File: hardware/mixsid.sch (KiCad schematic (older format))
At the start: 71 parts, among them P1 INPUT, P2 CONTROL, P3 RAW, P4 SOCKET LEFT, P5 OUTPUT, P6 SOCKET RIGHT, P7 -5V, Q1 BC547, Q2 BC547, U1 GAL16V8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

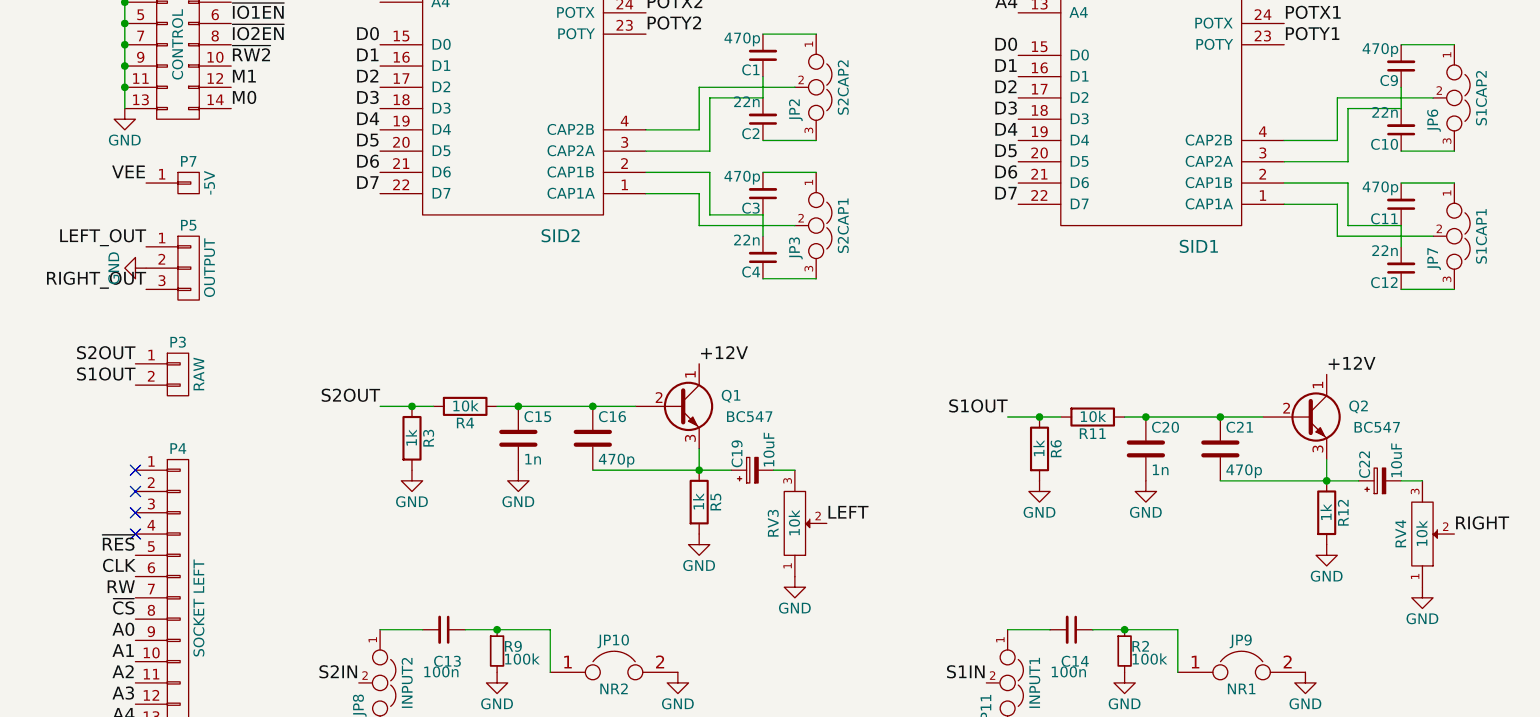
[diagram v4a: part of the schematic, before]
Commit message: Hardware: Added R8 Jumpers, Feed SID specific VDD into output stages
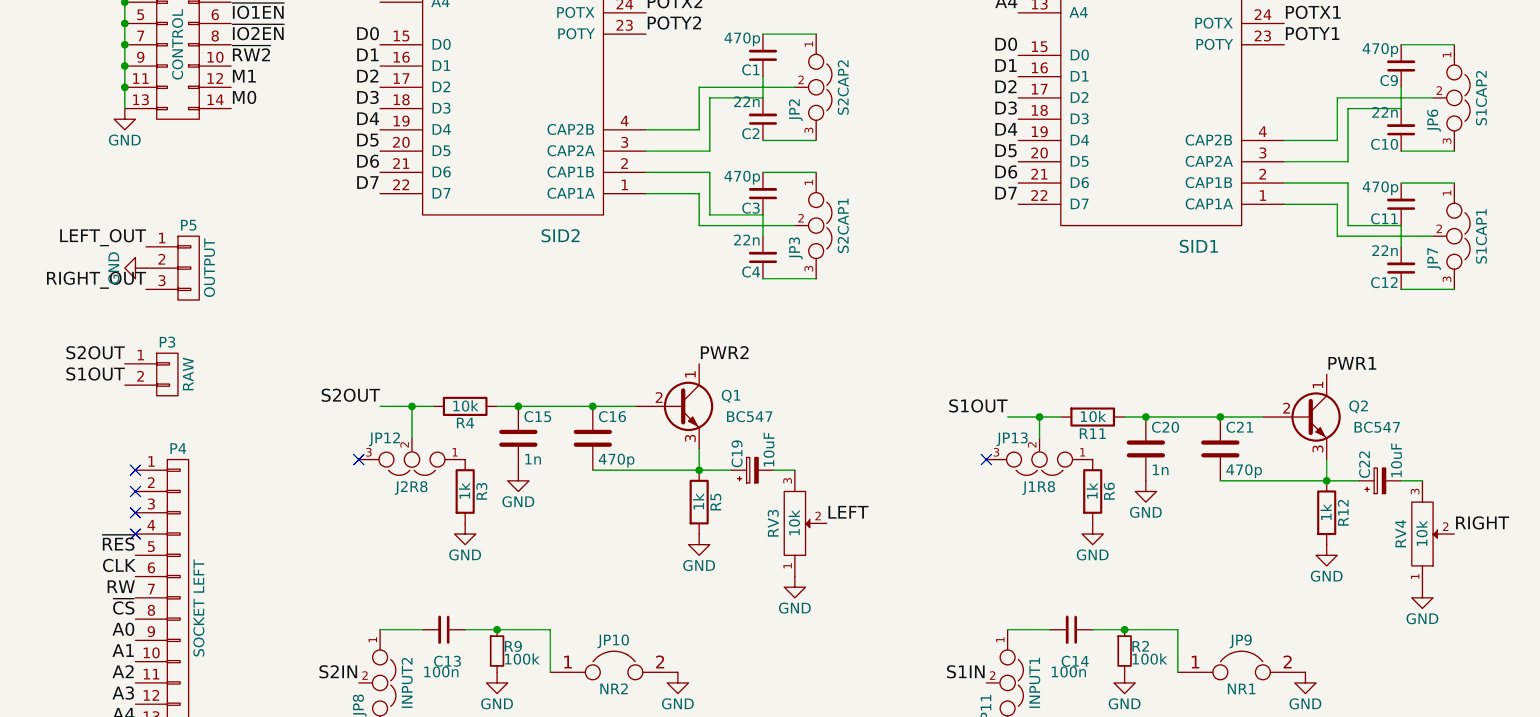
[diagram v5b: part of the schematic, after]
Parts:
- removed P7: -5V, Measurement_Points:Measurement_Point_Round-TH_Small, symbol CONN_01X01
- added JP12: J2R8, Pinheaders:Pin_Header_Straight_1x03_Pitch2.00mm, symbol JUMPER3
- added JP13: J1R8, Pinheaders:Pin_Header_Straight_1x03_Pitch2.00mm, symbol JUMPER3
- JP1, JP11, JP2, JP3, JP5, JP6, JP7, JP8: footprint Pinheaders:Pin_Header_Straight_1x03 -> Pinheaders:Pin_Header_Straight_1x03_Pitch2.00mm
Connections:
- net +12V: no longer Q1.1 (C), Q2.1 (C)
- net PWR1: now also Q2.1 (C)
- net PWR2: now also Q1.1 (C)
- net S1OUT: now also JP13.2; no longer R6.1
- net S2OUT: now also JP12.2; no longer R3.1
- new net: JP12.1, R3.1
- new net: JP13.1, R6.1
- no-connect marks 12 -> 14
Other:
- moved on the sheet: R3, R6
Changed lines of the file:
@@
 F 0 "JP2" H 4250 2150 50  0000 L CNN
 F 1 "S2CAP2" H 4200 2350 50  0000 C BNN
-F 2 "Pinheaders:Pin_Header_Straight_1x03" H 4200 2250 60  0001 C CNN
+F 2 "Pinheaders:Pin_Header_Straight_1x03_Pitch2.00mm" H 4200 2250 60  0001 C CNN
 F 3 "" H 4200 2250 60  0000 C CNN
 	1    4200 2250
@@
 F 0 "JP3" H 4250 2800 50  0000 L CNN
 F 1 "S2CAP1" H 4200 3000 50  0000 C BNN
-F 2 "Pinheaders:Pin_Header_Straight_1x03" H 4200 2900 60  0001 C CNN
+F 2 "Pinheaders:Pin_Header_Straight_1x03_Pitch2.00mm" H 4200 2900 60  0001 C CNN
 F 3 "" H 4200 2900 60  0000 C CNN
 	1    4200 2900
@@
 F 0 "JP6" H 7250 2200 50  0000 L CNN
 F 1 "S1CAP2" H 7200 2400 50  0000 C BNN
-F 2 "Pinheaders:Pin_Header_Straight_1x03" H 7200 2300 60  0001 C CNN
+F 2 "Pinheaders:Pin_Header_Straight_1x03_Pitch2.00mm" H 7200 2300 60  0001 C CNN
 F 3 "" H 7200 2300 60  0000 C CNN
 	1    7200 2300
@@
 F 0 "JP7" H 7250 2850 50  0000 L CNN
 F 1 "S1CAP1" H 7200 3050 50  0000 C BNN
-F 2 "Pinheaders:Pin_Header_Straight_1x03" H 7200 2950 60  0001 C CNN
+F 2 "Pinheaders:Pin_Header_Straight_1x03_Pitch2.00mm" H 7200 2950 60  0001 C CNN
 F 3 "" H 7200 2950 60  0000 C CNN
 	1    7200 2950
@@
 F 0 "JP1" H 4100 850 50  0000 L CNN
 F 1 "SUPPLY2" H 4050 1050 50  0000 C BNN
-F 2 "Pinheaders:Pin_Header_Straight_1x03" H 4050 950 60  0001 C CNN
+F 2 "Pinheaders:Pin_Header_Straight_1x03_Pitch2.00mm" H 4050 950 60  0001 C CNN
 F 3 "" H 4050 950 60  0000 C CNN
 	1    4050 950
@@
 F 0 "JP5" H 7100 900 50  0000 L CNN
 F 1 "SUPPLY1" H 7050 1100 50  0000 C BNN
-F 2 "Pinheaders:Pin_Header_Straight_1x03" H 7050 1000 60  0001 C CNN
+F 2 "Pinheaders:Pin_Header_Straight_1x03_Pitch2.00mm" H 7050 1000 60  0001 C CNN
 F 3 "" H 7050 1000 60  0000 C CNN
 	1    7050 1000
@@
 F 0 "JP11" H 5150 4950 50  0000 L CNN
 F 1 "INPUT1" H 5100 5150 50  0000 C BNN
-F 2 "Pinheaders:Pin_Header_Straight_1x03" H 5100 5050 60  0001 C CNN
+F 2 "Pinheaders:Pin_Header_Straight_1x03_Pitch2.00mm" H 5100 5050 60  0001 C CNN
 F 3 "" H 5100 5050 60  0000 C CNN
 	1    5100 5050
@@
 F 0 "JP8" H 2200 4950 50  0000 L CNN
 F 1 "INPUT2" H 2150 5150 50  0000 C BNN
-F 2 "Pinheaders:Pin_Header_Straight_1x03" H 2150 5050 60  0001 C CNN
+F 2 "Pinheaders:Pin_Header_Straight_1x03_Pitch2.00mm" H 2150 5050 60  0001 C CNN
 F 3 "" H 2150 5050 60  0000 C CNN
 	1    2150 5050
@@
 L R R3
 U 1 1 56E6AAD9
-P 2300 3900
-F 0 "R3" V 2380 3900 50  0000 C CNN
-F 1 "1k" V 2300 3900 50  0000 C CNN
-F 2 "Discret:R1" V 2230 3900 30  0001 C CNN
-F 3 "" H 2300 3900 30  0000 C CNN
-	1    2300 3900
+P 2550 4150
+F 0 "R3" V 2630 4150 50  0000 C CNN
+F 1 "1k" V 2550 4150 50  0000 C CNN
+F 2 "Discret:R1" V 2480 4150 30  0001 C CNN
+F 3 "" H 2550 4150 30  0000 C CNN
+	1    2550 4150
 	1    0    0    -1
 $EndComp
@@
 L GND #PWR025
 U 1 1 56E6AC40
-P 2300 4050
-F 0 "#PWR025" H 2300 3800 50  0001 C CNN
-F 1 "GND" H 2300 3900 50  0000 C CNN
-F 2 "" H 2300 4050 60  0000 C CNN
-F 3 "" H 2300 4050 60  0000 C CNN
-	1    2300 4050
+P 2550 4300
+F 0 "#PWR025" H 2550 4050 50  0001 C CNN
+F 1 "GND" H 2550 4150 50  0000 C CNN
+F 2 "" H 2550 4300 60  0000 C CNN
+F 3 "" H 2550 4300 60  0000 C CNN
+	1    2550 4300
 	1    0    0    -1
 $EndComp
@@
 $EndComp
 Connection ~ 3150 3750
-Text Label 3650 3550 0    60   ~ 0
-+12V
 $Comp
 L R R5
@@
 L R R6
 U 1 1 56E6CA27
-P 5250 3950
-F 0 "R6" V 5330 3950 50  0000 C CNN
-F 1 "1k" V 5250 3950 50  0000 C CNN
-F 2 "Discret:R1" V 5180 3950 30  0001 C CNN
-F 3 "" H 5250 3950 30  0000 C CNN
-	1    5250 3950
+P 5500 4150
+F 0 "R6" V 5580 4150 50  0000 C CNN
+F 1 "1k" V 5500 4150 50  0000 C CNN
+F 2 "Discret:R1" V 5430 4150 30  0001 C CNN
+F 3 "" H 5500 4150 30  0000 C CNN
+	1    5500 4150
 	1    0    0    -1
 $EndComp
@@
 L GND #PWR028
 U 1 1 56E6CA2D
-P 5250 4100
-F 0 "#PWR028" H 5250 3850 50  0001 C CNN
-F 1 "GND" H 5250 3950 50  0000 C CNN
-F 2 "" H 5250 4100 60  0000 C CNN
-F 3 "" H 5250 4100 60  0000 C CNN
-	1    5250 4100
+P 5500 4300
+F 0 "#PWR028" H 5500 4050 50  0001 C CNN
+F 1 "GND" H 5500 4150 50  0000 C CNN
+F 2 "" H 5500 4300 60  0000 C CNN
+F 3 "" H 5500 4300 60  0000 C CNN
+	1    5500 4300
 	1    0    0    -1
 $EndComp
@@
 $EndComp
 Connection ~ 6100 3800
-Text Label 6600 3600 0    60   ~ 0
-+12V
 $Comp
 L R R12
@@
 Text Label 1450 2150 0    60   ~ 0
 ~RW2
+Text Label 3650 3550 0    60   ~ 0
+PWR2
+Text Label 6600 3600 0    60   ~ 0
+PWR1
+$Comp
+L JUMPER3 JP12
+U 1 1 573AF883
+P 2300 4000
+F 0 "JP12" H 2350 3900 50  0000 L CNN
+F 1 "J2R8" H 2300 4100 50  0000 C BNN
+F 2 "Pinheaders:Pin_Header_Straight_1x03_Pitch2.00mm" H 2300 4000 60  0001 C CNN
+F 3 "" H 2300 4000 60  0000 C CNN
+	1    2300 4000
+	-1   0    0    1
+$EndComp
+NoConn ~ 2050 4000
+Wire Wire Line
+	2300 3750 2300 3900
+$Comp
+L JUMPER3 JP13
+U 1 1 573B05C3
+P 5250 4000
+F 0 "JP13" H 5300 3900 50  0000 L CNN
+F 1 "J1R8" H 5250 4100 50  0000 C BNN
+F 2 "Pinheaders:Pin_Header_Straight_1x03_Pitch2.00mm" H 5250 4000 60  0001 C CNN
+F 3 "" H 5250 4000 60  0000 C CNN
+	1    5250 4000
+	-1   0    0    1
+$EndComp
+Wire Wire Line
+	5250 3900 5250 3800
+NoConn ~ 5000 4000
 $Comp
 L CONN_01X02 P3
-U 1 1 5732EF33
-P 1200 3600
-F 0 "P3" H 1200 3750 50  0000 C CNN
-F 1 "RAW" V 1300 3600 50  0000 C CNN
-F 2 "Pinheaders:Pin_Header_Straight_1x02" H 1200 3600 60  0001 C CNN
-F 3 "" H 1200 3600 60  0000 C CNN
-	1    1200 3600
-	1    0    0    -1
-$EndComp
-Text Label 1000 3550 2    60   ~ 0
+U 1 1 573B4485
+P 1150 3600
+F 0 "P3" H 1150 3750 50  0000 C CNN
+F 1 "RAW" V 1250 3600 50  0000 C CNN
+F 2 "Pinheaders:Pin_Header_Straight_1x02" H 1150 3600 60  0001 C CNN
+F 3 "" H 1150 3600 60  0000 C CNN
+	1    1150 3600
+	1    0    0    -1
+$EndComp
+Text Label 950  3550 2    60   ~ 0
 S2OUT
-Text Label 1000 3650 2    60   ~ 0
+Text Label 950  3650 2    60   ~ 0
 S1OUT
-$Comp
-L CONN_01X01 P7
-U 1 1 57334D37
-P 1250 2700
-F 0 "P7" H 1250 2800 50  0000 C CNN
-F 1 "-5V" V 1350 2700 50  0000 C CNN
-F 2 "Measurement_Points:Measurement_Point_Round-TH_Small" H 1250 2700 60  0001 C CNN
-F 3 "" H 1250 2700 60  0000 C CNN
-	1    1250 2700
-	1    0    0    -1
-$EndComp
-Text Label 1050 2700 2    60   ~ 0
-VEE
 $EndSCHEMATC

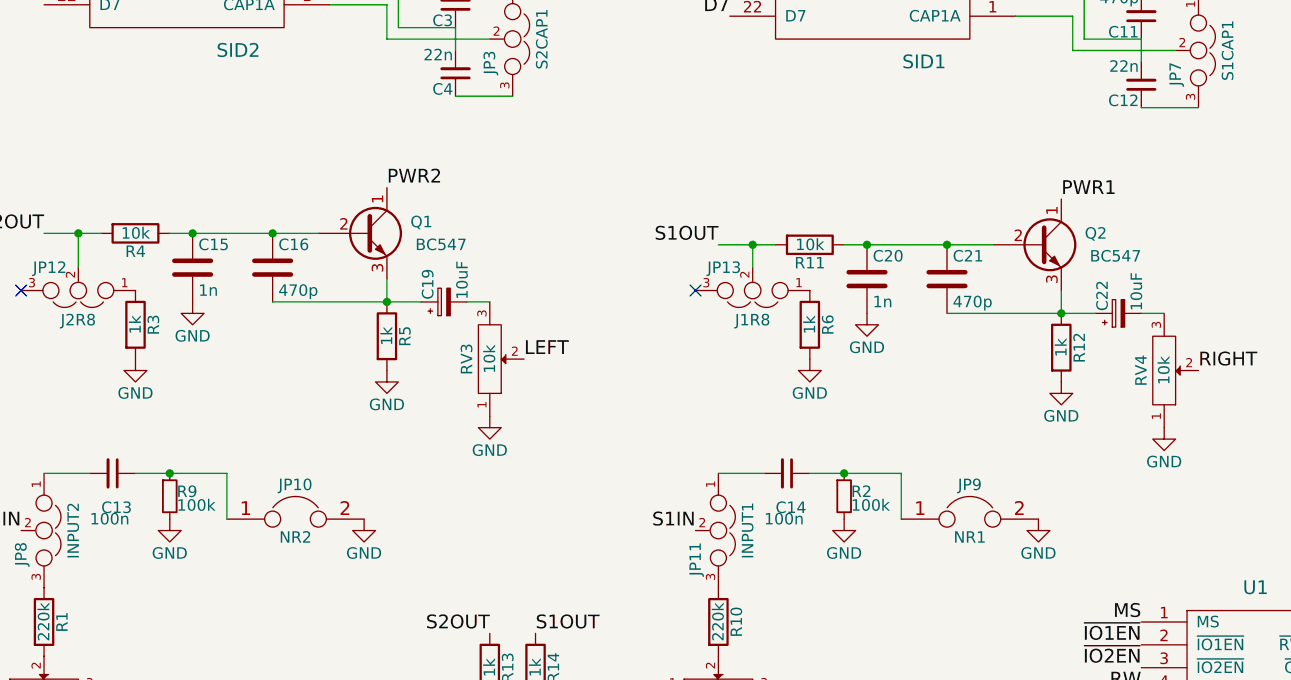
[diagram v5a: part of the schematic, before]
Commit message: Hardware: Reverted to +12V for both output stages, rerouted, refined
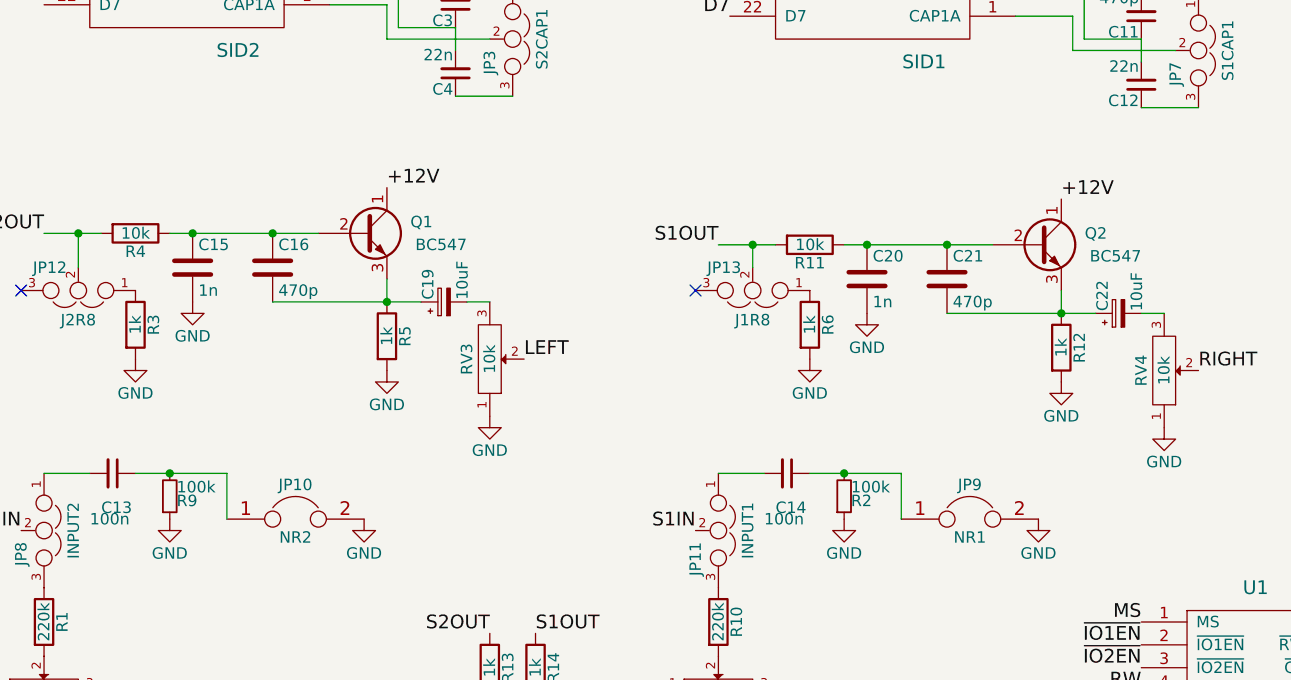
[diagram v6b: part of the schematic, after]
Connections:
- net +12V: now also Q1.1 (C), Q2.1 (C)
- net GND: now also R2.1, R9.1; no longer R2.2, R9.2
- net PWR1: no longer Q2.1 (C)
- net PWR2: no longer Q1.1 (C)
- net at C14.1, JP9.1: now also R2.2; no longer R2.1
- net at C13.1, JP10.1: now also R9.2; no longer R9.1
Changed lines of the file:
@@
 F 3 "" H 5650 4900 60  0000 C CNN
 	1    5650 4900
-	1    0    0    -1
+	1    0    0    1
 $EndComp
 $Comp
@@
 F 3 "" H 2700 4900 60  0000 C CNN
 	1    2700 4900
-	1    0    0    -1
+	1    0    0    1
 $EndComp
 $Comp
@@
 Text Label 1450 2150 0    60   ~ 0
 ~RW2
-Text Label 3650 3550 0    60   ~ 0
-PWR2
-Text Label 6600 3600 0    60   ~ 0
-PWR1
 $Comp
 L JUMPER3 JP12
@@
 Text Label 950  3650 2    60   ~ 0
 S1OUT
+Text Label 3650 3550 0    60   ~ 0
++12V
+Text Label 6600 3600 0    60   ~ 0
++12V
 $EndSCHEMATC
